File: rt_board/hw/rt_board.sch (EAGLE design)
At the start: 64 parts, among them IC1 MCP170333MB, IC2/L1 TLE4935L, IC3/L2 TLE4935L, IC4/L1 TLE4935L, IC5/L2 TLE4935L, Q1 8MHz, U1 STM32F051R8T7, U2 SN74AVC4T245PW, U3 DRV8801PWP, U4 ACS712ELCTR-20A-T, U5 DRV8801PWP, U6 ACS712ELCTR-20A-T, U7 2N7002BKW, X1 PWR, X2 LEFT, X3 RIGHT

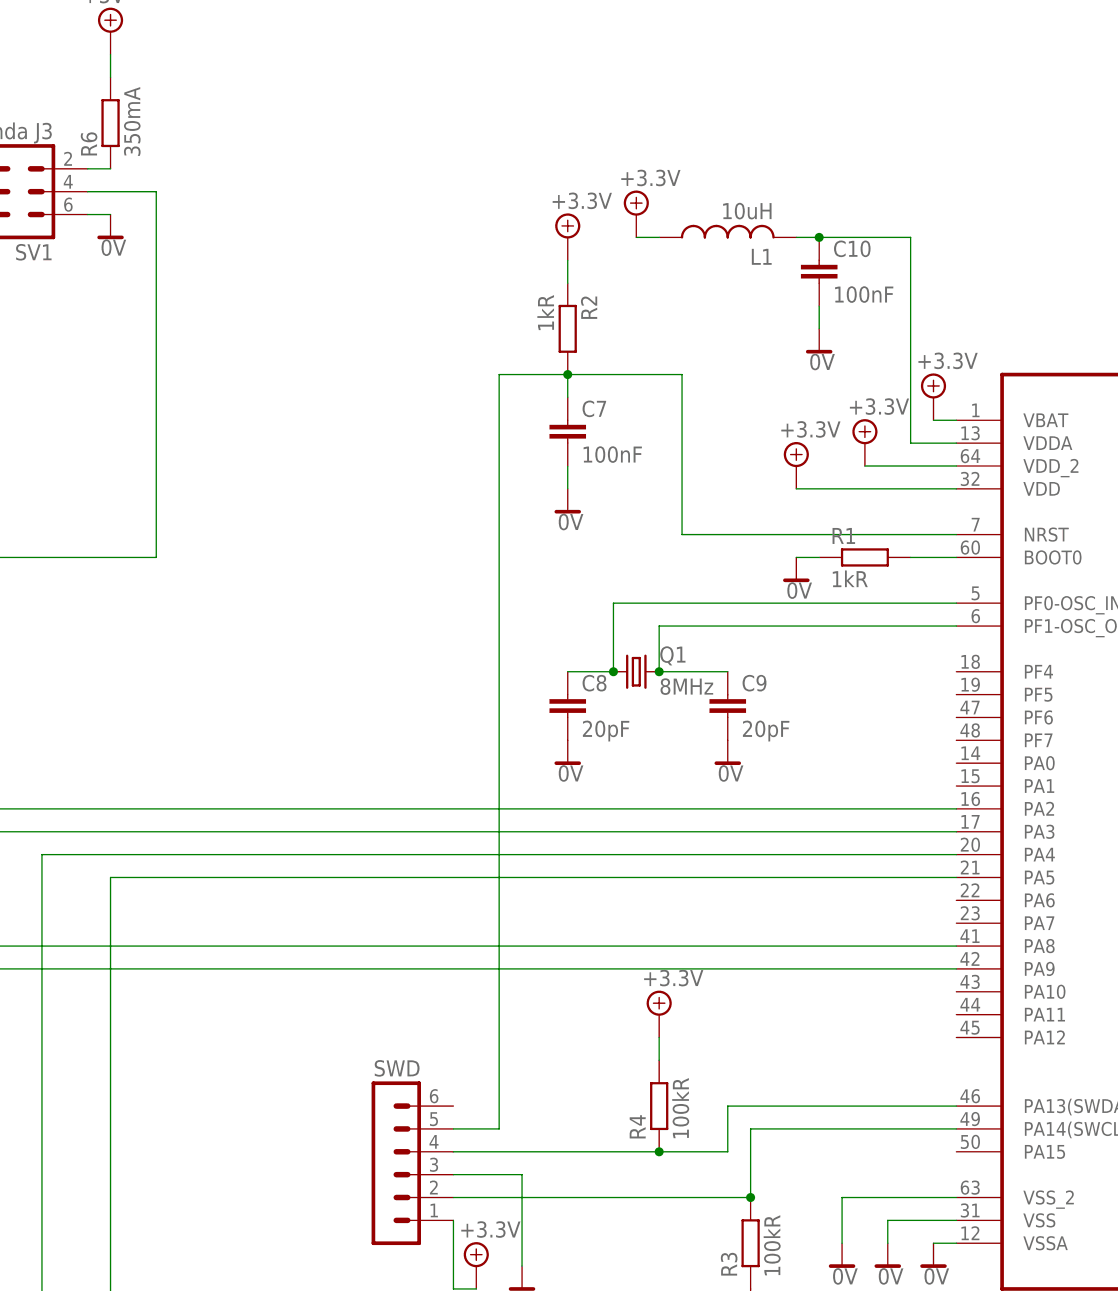
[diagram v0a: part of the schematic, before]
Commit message: added boot0 and reset switches
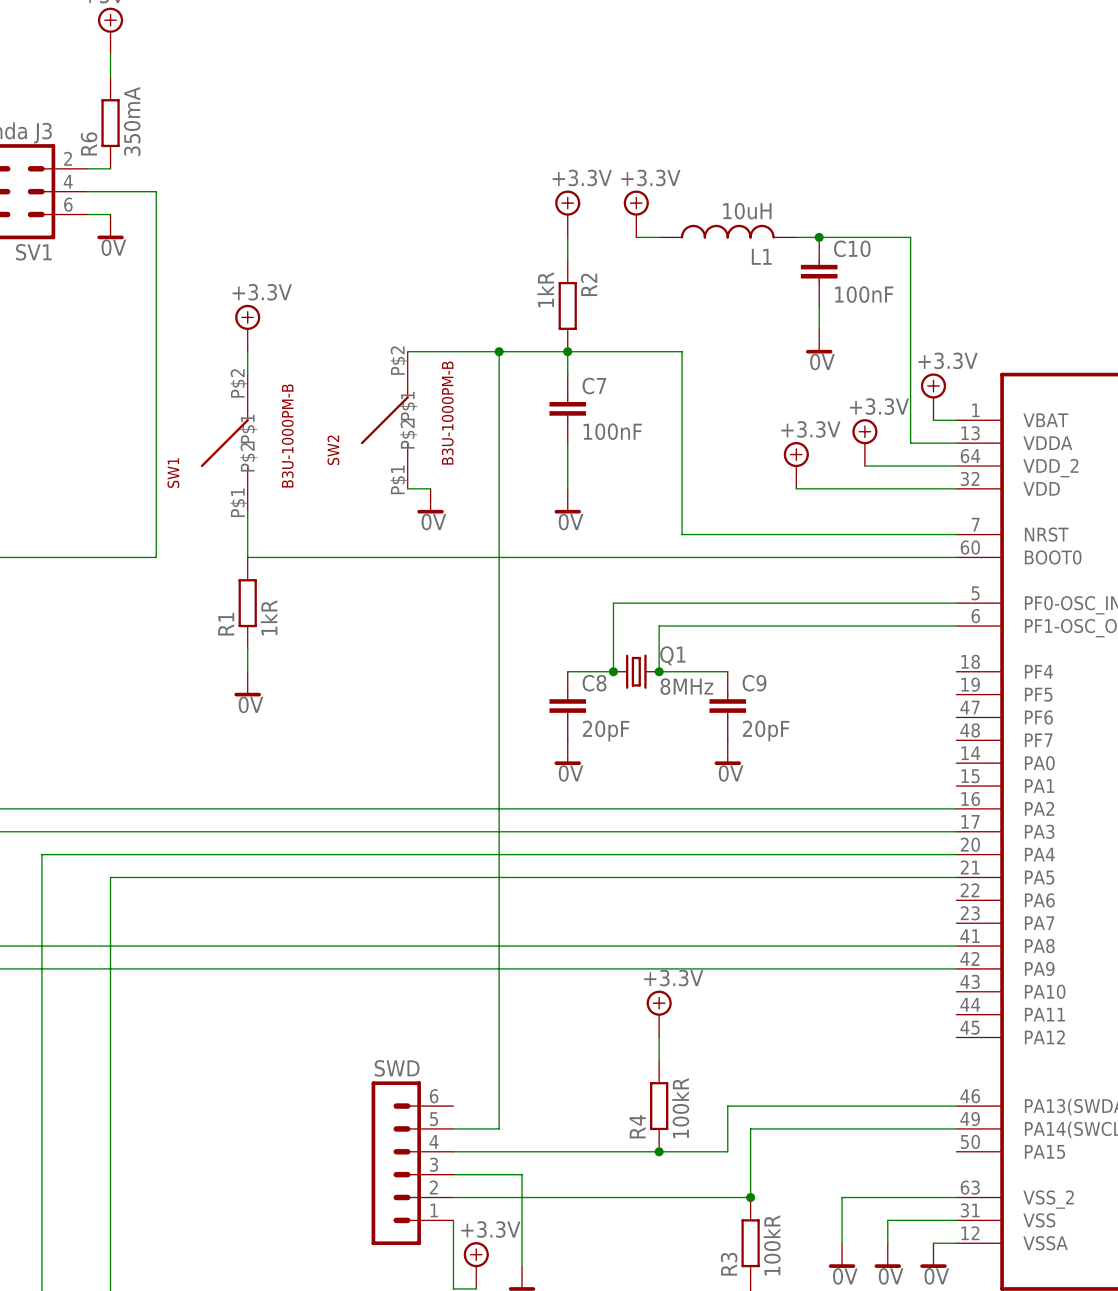
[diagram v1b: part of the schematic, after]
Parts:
- added SW1, SW2: B3U-1000PM-B, basz:B3U-1000PM-B
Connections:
- net +5V: now also SW1.P$2
- net 0V: now also SW2.P$1
- net N$5: now also SW1.P$1
- net N$6: now also SW2.P$2
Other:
- moved on the sheet: C7, R1, R2
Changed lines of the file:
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@@
 <part name="LED2" library="led" deviceset="LED" device="CHIPLED_0603" value="GREEN"/>
 <part name="SUPPLY84" library="supply2" deviceset="+5V" device="" value="+3.3V"/>
+<part name="SW1" library="basz" deviceset="B3U-1000PM-B" device=""/>
+<part name="SW2" library="basz" deviceset="B3U-1000PM-B" device=""/>
+<part name="SUPPLY85" library="supply2" deviceset="+5V" device="" value="+3.3V"/>
+<part name="SUPPLY86" library="supply2" deviceset="0V" device=""/>
 </parts>
 <sheets>
@@
 <instance part="SUPPLY8" gate="+5V" x="30.48" y="147.32"/>
 <instance part="SUPPLY9" gate="0V" x="30.48" y="134.62"/>
-<instance part="R1" gate="G$1" x="-35.56" y="71.12"/>
-<instance part="SUPPLY10" gate="0V" x="-43.18" y="68.58"/>
-<instance part="R2" gate="G$1" x="-68.58" y="96.52" rot="R270"/>
-<instance part="C7" gate="G$1" x="-68.58" y="86.36"/>
+<instance part="R1" gate="G$1" x="-104.14" y="66.04" rot="R90"/>
+<instance part="SUPPLY10" gate="0V" x="-104.14" y="55.88"/>
+<instance part="R2" gate="G$1" x="-68.58" y="99.06" rot="R270"/>
+<instance part="C7" gate="G$1" x="-68.58" y="88.9"/>
 <instance part="Q1" gate="G$1" x="-60.96" y="58.42"/>
 <instance part="SUPPLY11" gate="0V" x="-68.58" y="76.2"/>
-<instance part="SUPPLY12" gate="+5V" x="-68.58" y="106.68"/>
+<instance part="SUPPLY12" gate="+5V" x="-68.58" y="109.22"/>
 <instance part="C8" gate="G$1" x="-68.58" y="55.88"/>
 <instance part="C9" gate="G$1" x="-50.8" y="55.88"/>
@@
 <instance part="LED2" gate="G$1" x="114.3" y="124.46"/>
 <instance part="SUPPLY84" gate="+5V" x="114.3" y="132.08"/>
+<instance part="SW1" gate="G$1" x="-104.14" y="83.82" rot="R90"/>
+<instance part="SW2" gate="G$1" x="-86.36" y="86.36" rot="R90"/>
+<instance part="SUPPLY85" gate="+5V" x="-104.14" y="96.52"/>
+<instance part="SUPPLY86" gate="0V" x="-83.82" y="76.2"/>
 </instances>
 <busses>
@@
 <pinref part="R1" gate="G$1" pin="1"/>
 <pinref part="SUPPLY10" gate="0V" pin="0V"/>
-<wire x1="-43.18" y1="71.12" x2="-40.64" y2="71.12" width="0.1524" layer="91"/>
+<wire x1="-104.14" y1="58.42" x2="-104.14" y2="60.96" width="0.1524" layer="91"/>
 </segment>
 <segment>
 <pinref part="C7" gate="G$1" pin="2"/>
 <pinref part="SUPPLY11" gate="0V" pin="0V"/>
-<wire x1="-68.58" y1="81.28" x2="-68.58" y2="78.74" width="0.1524" layer="91"/>
+<wire x1="-68.58" y1="83.82" x2="-68.58" y2="78.74" width="0.1524" layer="91"/>
 </segment>
 <segment>
@@
 <pinref part="SUPPLY83" gate="0V" pin="0V"/>
 <wire x1="73.66" y1="111.76" x2="78.74" y2="111.76" width="0.1524" layer="91"/>
+</segment>
+<segment>
+<pinref part="SW2" gate="G$1" pin="P$1"/>
+<pinref part="SUPPLY86" gate="0V" pin="0V"/>
+<wire x1="-86.36" y1="78.74" x2="-83.82" y2="78.74" width="0.1524" layer="91"/>
 </segment>
 </net>
@@
 <pinref part="R2" gate="G$1" pin="1"/>
 <pinref part="SUPPLY12" gate="+5V" pin="+5V"/>
-<wire x1="-68.58" y1="104.14" x2="-68.58" y2="101.6" width="0.1524" layer="91"/>
+<wire x1="-68.58" y1="106.68" x2="-68.58" y2="104.14" width="0.1524" layer="91"/>
 </segment>
 <segment>
@@
 <pinref part="SUPPLY84" gate="+5V" pin="+5V"/>
 <wire x1="114.3" y1="129.54" x2="114.3" y2="127" width="0.1524" layer="91"/>
+</segment>
+<segment>
+<pinref part="SW1" gate="G$1" pin="P$2"/>
+<pinref part="SUPPLY85" gate="+5V" pin="+5V"/>
+<wire x1="-104.14" y1="91.44" x2="-104.14" y2="93.98" width="0.1524" layer="91"/>
 </segment>
 </net>
@@
 <pinref part="U1" gate="A" pin="BOOT0"/>
 <pinref part="R1" gate="G$1" pin="2"/>
-<wire x1="-30.48" y1="71.12" x2="-25.4" y2="71.12" width="0.1524" layer="91"/>
+<wire x1="-104.14" y1="71.12" x2="-25.4" y2="71.12" width="0.1524" layer="91"/>
+<pinref part="SW1" gate="G$1" pin="P$1"/>
+<wire x1="-104.14" y1="76.2" x2="-104.14" y2="71.12" width="0.1524" layer="91"/>
 </segment>
 </net>
@@
 <pinref part="U1" gate="A" pin="NRST"/>
 <pinref part="R2" gate="G$1" pin="2"/>
-<wire x1="-68.58" y1="91.44" x2="-55.88" y2="91.44" width="0.1524" layer="91"/>
-<wire x1="-55.88" y1="91.44" x2="-55.88" y2="73.66" width="0.1524" layer="91"/>
+<wire x1="-68.58" y1="93.98" x2="-55.88" y2="93.98" width="0.1524" layer="91"/>
+<wire x1="-55.88" y1="93.98" x2="-55.88" y2="73.66" width="0.1524" layer="91"/>
 <wire x1="-55.88" y1="73.66" x2="-25.4" y2="73.66" width="0.1524" layer="91"/>
 <pinref part="C7" gate="G$1" pin="1"/>
-<junction x="-68.58" y="91.44"/>
+<junction x="-68.58" y="93.98"/>
 <pinref part="SWD" gate="1" pin="5"/>
 <wire x1="-81.28" y1="7.62" x2="-76.2" y2="7.62" width="0.1524" layer="91"/>
-<wire x1="-76.2" y1="7.62" x2="-76.2" y2="91.44" width="0.1524" layer="91"/>
-<wire x1="-76.2" y1="91.44" x2="-68.58" y2="91.44" width="0.1524" layer="91"/>
-<wire x1="-68.58" y1="91.44" x2="-68.58" y2="88.9" width="0.1524" layer="91"/>
+<wire x1="-76.2" y1="7.62" x2="-76.2" y2="93.98" width="0.1524" layer="91"/>
+<wire x1="-76.2" y1="93.98" x2="-68.58" y2="93.98" width="0.1524" layer="91"/>
+<wire x1="-68.58" y1="93.98" x2="-68.58" y2="91.44" width="0.1524" layer="91"/>
+<pinref part="SW2" gate="G$1" pin="P$2"/>
+<wire x1="-86.36" y1="93.98" x2="-76.2" y2="93.98" width="0.1524" layer="91"/>
+<junction x="-76.2" y="93.98"/>
 </segment>
 </net>

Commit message: changed quartz package
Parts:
- Q1: device crystal:CRYSTALSM49 -> crystal:MC-405
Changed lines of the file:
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@@
 <part name="R2" library="rcl" deviceset="R-EU_" device="R0603" value="1kR"/>
 <part name="C7" library="rcl" deviceset="C-EU" device="C1206" value="100nF"/>
-<part name="Q1" library="crystal" deviceset="CRYSTAL" device="SM49" value="8MHz"/>
+<part name="Q1" library="crystal" deviceset="MC-405" device="" value="8MHz"/>
 <part name="SUPPLY11" library="supply2" deviceset="0V" device=""/>
 <part name="SUPPLY12" library="supply2" deviceset="+5V" device="" value="+3.3V"/>
@@
 <instance part="R2" gate="G$1" x="-68.58" y="99.06" rot="R270"/>
 <instance part="C7" gate="G$1" x="-68.58" y="88.9"/>
-<instance part="Q1" gate="G$1" x="-60.96" y="58.42"/>
+<instance part="Q1" gate="P" x="-60.96" y="58.42"/>
 <instance part="SUPPLY11" gate="0V" x="-68.58" y="76.2"/>
 <instance part="SUPPLY12" gate="+5V" x="-68.58" y="109.22"/>
@@
 <net name="N$7" class="0">
 <segment>
-<pinref part="Q1" gate="G$1" pin="1"/>
+<pinref part="Q1" gate="P" pin="1"/>
 <pinref part="C8" gate="G$1" pin="1"/>
 <wire x1="-68.58" y1="58.42" x2="-63.5" y2="58.42" width="0.1524" layer="91"/>
@@
 <net name="N$8" class="0">
 <segment>
-<pinref part="Q1" gate="G$1" pin="2"/>
+<pinref part="Q1" gate="P" pin="2"/>
 <pinref part="C9" gate="G$1" pin="1"/>
 <wire x1="-50.8" y1="58.42" x2="-58.42" y2="58.42" width="0.1524" layer="91"/>

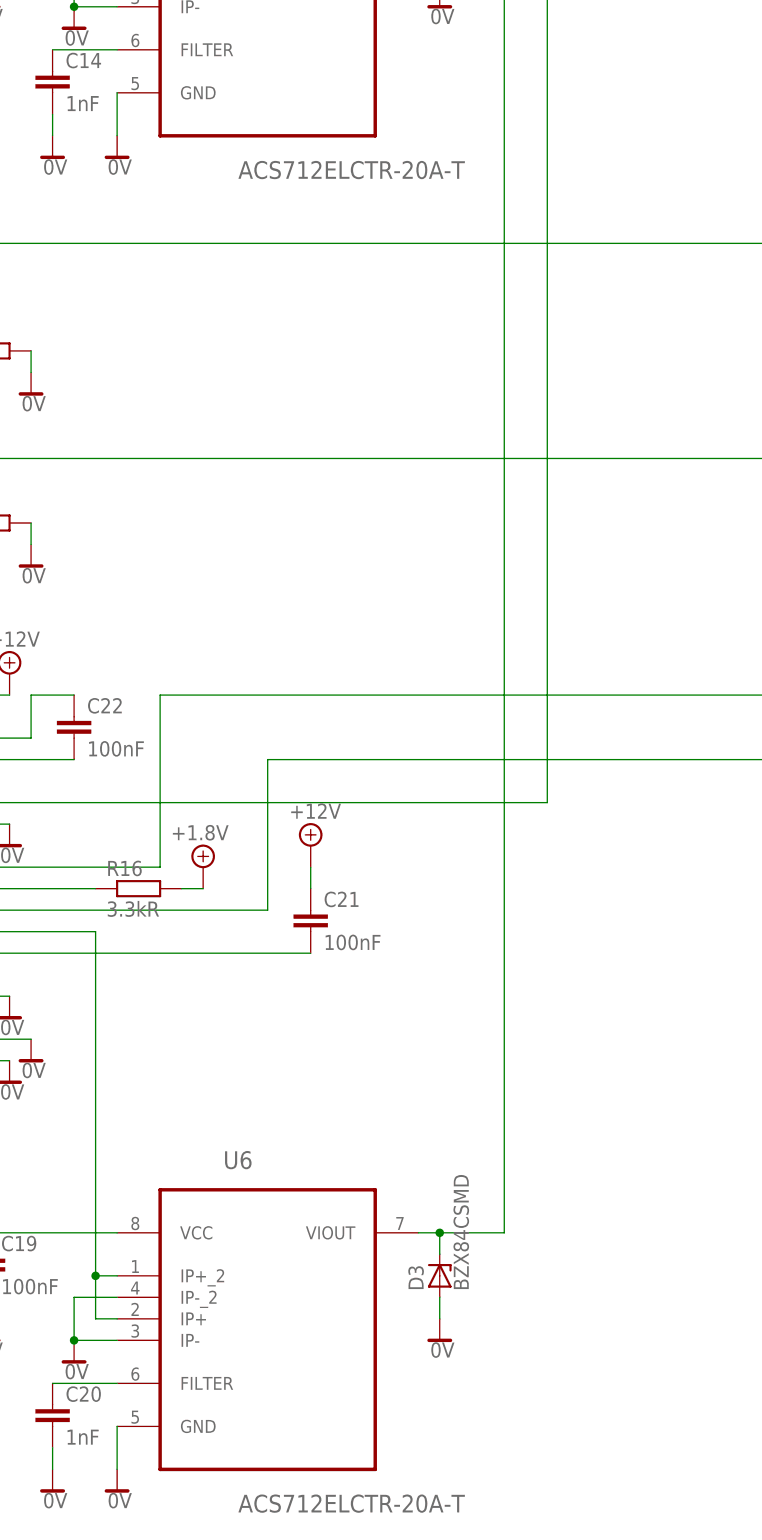
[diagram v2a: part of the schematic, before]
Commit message: replaced ACS712ELCTR-20A-T with more acurate in a given range ACS712ELCTR-05B-T
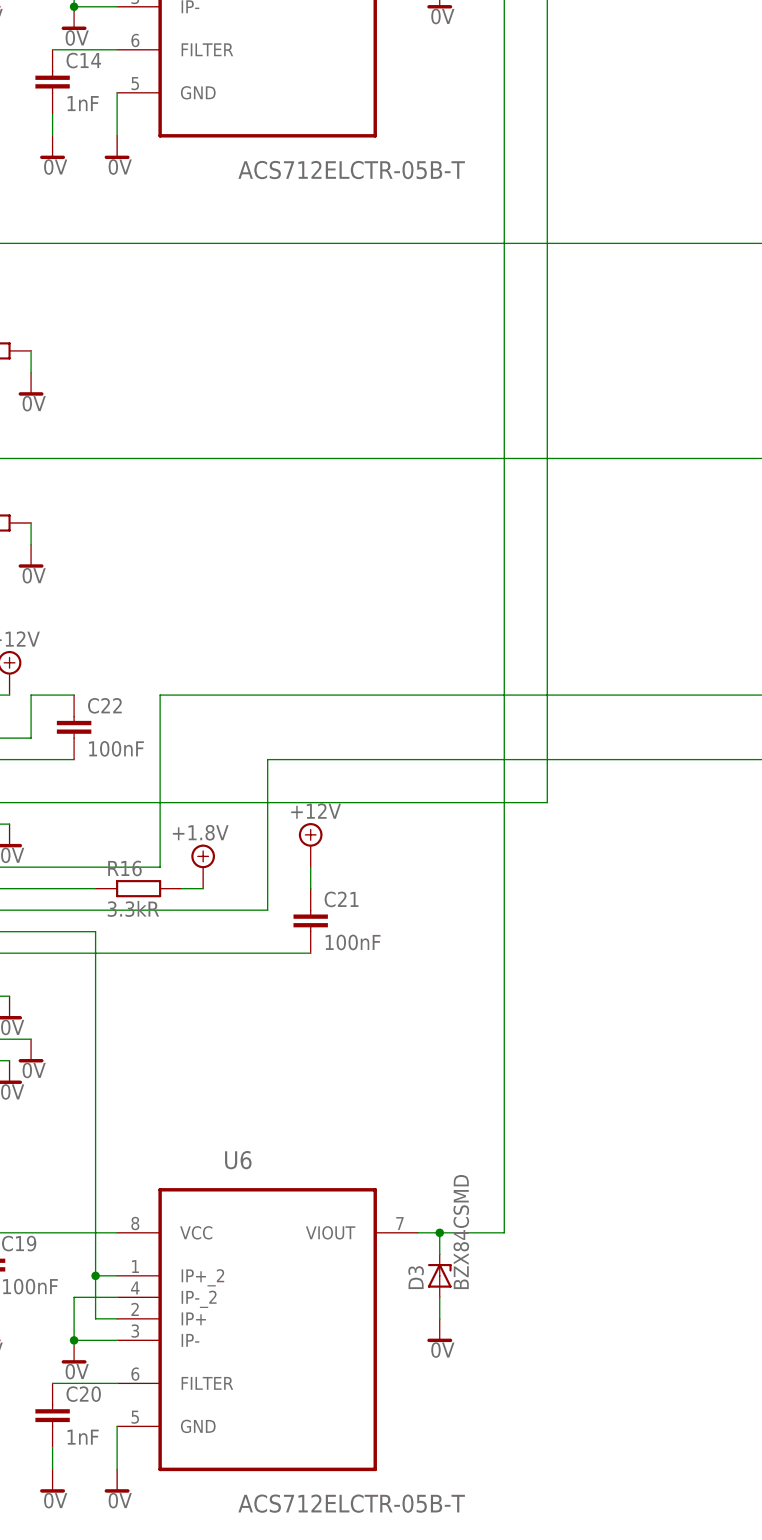
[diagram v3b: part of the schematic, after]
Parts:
- U4, U6: value ACS712ELCTR-20A-T -> ACS712ELCTR-05B-T
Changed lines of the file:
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@@
 <part name="SUPPLY48" library="supply2" deviceset="+12V" device=""/>
 <part name="SUPPLY49" library="supply2" deviceset="0V" device=""/>
-<part name="U4" library="Allegro-ACS712ELCTR-20A-T" deviceset="ACS712ELCTR-20A-T" device=""/>
+<part name="U4" library="Allegro-ACS712ELCTR-20A-T" deviceset="ACS712ELCTR-20A-T" device="" value="ACS712ELCTR-05B-T"/>
 <part name="C13" library="rcl" deviceset="C-EU" device="C1206" value="100nF"/>
 <part name="C14" library="rcl" deviceset="C-EU" device="C1206" value="1nF"/>
@@
 <part name="SUPPLY69" library="supply2" deviceset="+12V" device=""/>
 <part name="SUPPLY70" library="supply2" deviceset="0V" device=""/>
-<part name="U6" library="Allegro-ACS712ELCTR-20A-T" deviceset="ACS712ELCTR-20A-T" device=""/>
+<part name="U6" library="Allegro-ACS712ELCTR-20A-T" deviceset="ACS712ELCTR-20A-T" device="" value="ACS712ELCTR-05B-T"/>
 <part name="C19" library="rcl" deviceset="C-EU" device="C1206" value="100nF"/>
 <part name="C20" library="rcl" deviceset="C-EU" device="C1206" value="1nF"/>
